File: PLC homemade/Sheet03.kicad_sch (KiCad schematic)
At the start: 54 parts, among them J1 M20-7820646, J16 Conn_01x04, J17 Conn_01x02, U11 GP8403-TC50-EW_C3152007, U12 MAX13487EESAT, U13 SMBJ7.0CA-Q, U14 SMBJ7.0CA-Q, U4 LM324ADT, U5 SN74LVC1G125DRL, U6 SN74LVC1G125DRL

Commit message: :tada: Run Electrical rule checker All errors corrected
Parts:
- C21, C22, C23, C24, C25, C26, C28, C42, C43, C45, C46: footprint (none) -> Capacitor_SMD:C_01005_0402Metric
- C27, C41, C44, C47, C48: footprint (none) -> Capacitor_SMD:C_0201_0603Metric
- J1: footprint (none) -> M20-7820646:HARWIN_M20-7820646
- J16: footprint (none) -> Connector_PinHeader_2.00mm:PinHeader_1x04_P2.00mm_Vertical
- J17: footprint (none) -> Connector_PinHeader_2.00mm:PinHeader_1x02_P2.00mm_Vertical
- L2, L3: footprint (none) -> Inductor_SMD:L_APV_APH1040
- R23, R29, R30, R32, R33, R34, R35, R66: footprint (none) -> Resistor_SMD:R_1206_3216Metric
- R24, R25, R26, R27, R28, R31, R65, R67, R68: footprint (none) -> Resistor_SMD:R_01005_0402Metric
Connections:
- net INPUT_AAA0 is gone; now on net INPUT_AA0: U4.2 (NEG_1)
- net INPUT_AAA1 is gone; now on net INPUT_AA1: U4.6 (NEG_2)
- net INPUT_AAA2 is gone; now on net INPUT_AA2: U4.9 (NEG3)
- net INPUT_AAA3 is gone; now on net INPUT_AA3: U4.13 (NEG_4)
- net AGND: now also U6.3 (GND)
- no-connect marks 0 -> 1
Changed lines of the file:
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@@
 		(color 0 0 0 0)
 	)
+	(no_connect
+		(at 231.14 266.7)
+	)
 	(wire
 		(pts
@@
 	(wire
 		(pts
+			(xy 232.41 213.36) (xy 232.41 215.9)
+		)
+		(stroke
+			(width 0)
+			(type default)
+		)
+	)
+	(wire
+		(pts
 			(xy 114.3 210.82) (xy 114.3 217.17)
 		)
@@
 		)
 	)
-	(label "INPUT_AAA0"
+	(label "INPUT_AA0"
 		(at 81.28 40.64 0)
 		(effects
@@
 		)
 	)
-	(label "INPUT_AAA1"
+	(label "INPUT_AA1"
 		(at 81.28 45.72 0)
 		(effects
@@
 		)
 	)
-	(label "INPUT_AAA2"
+	(label "INPUT_AA2"
 		(at 81.28 50.8 0)
 		(effects
@@
 		)
 	)
-	(label "INPUT_AAA3"
+	(label "INPUT_AA3"
 		(at 81.28 55.88 0)
 		(effects
@@
 		)
 	)
+	(global_label "4G_RX"
+		(shape input)
+		(at 223.52 261.62 180)
+		(fields_autoplaced yes)
+		(effects
+			(font
+				(size 1.27 1.27)
+			)
+			(justify right)
+		)
+		(property "Intersheetrefs" "${INTERSHEET_REFS}"
+			(at 214.6082 261.62 0)
+			(effects
+				(font
+					(size 1.27 1.27)
+				)
+				(justify right)
+				(hide yes)
+			)
+		)
+	)
 	(global_label "INA3"
 		(shape input)
@@
 		)
 	)
-	(hierarchical_label "4G_TX"
+	(global_label "4G_TX"
 		(shape input)
 		(at 223.52 264.16 180)
+		(fields_autoplaced yes)
 		(effects
 			(font
@@
 			(justify right)
 		)
-	)
-	(hierarchical_label "4G_RX"
-		(shape input)
-		(at 223.52 261.62 180)
-		(effects
-			(font
-				(size 1.27 1.27)
+		(property "Intersheetrefs" "${INTERSHEET_REFS}"
+			(at 214.9106 264.16 0)
+			(effects
+				(font
+					(size 1.27 1.27)
+				)
+				(justify right)
+				(hide yes)
 			)
-			(justify right)
 		)
 	)
@@
 			)
 		)
-		(property "Footprint" ""
+		(property "Footprint" "Capacitor_SMD:C_01005_0402Metric"
 			(at 139.3952 153.67 0)
 			(effects
@@
 			)
 		)
-		(property "Footprint" ""
+		(property "Footprint" "Inductor_SMD:L_APV_APH1040"
 			(at 38.1 129.54 0)
 			(effects
@@
 			)
 		)
-		(property "Footprint" ""
+		(property "Footprint" "Capacitor_SMD:C_01005_0402Metric"
 			(at 171.1452 157.48 0)
 			(effects
@@
 			)
 		)
-		(property "Footprint" ""
+		(property "Footprint" "Connector_PinHeader_2.00mm:PinHeader_1x04_P2.00mm_Vertical"
 			(at 177.8 91.44 0)
 			(effects
@@
 			)
 		)
-		(property "Footprint" ""
+		(property "Footprint" "Resistor_SMD:R_01005_0402Metric"
 			(at 188.722 39.37 90)
 			(effects
@@
 			)
 		)
-		(property "Footprint" ""
+		(property "Footprint" "Capacitor_SMD:C_01005_0402Metric"
 			(at 72.0852 140.97 0)
 			(effects
@@
 			)
 		)
-		(property "Footprint" ""
+		(property "Footprint" "Capacitor_SMD:C_01005_0402Metric"
 			(at 228.2952 41.91 0)
 			(effects
@@
 			)
 		)
-		(property "Footprint" ""
+		(property "Footprint" "Capacitor_SMD:C_0201_0603Metric"
 			(at 134.9248 121.92 0)
 			(effects
@@
 			)
 		)
-		(property "Footprint" ""
+		(property "Footprint" "Resistor_SMD:R_1206_3216Metric"
 			(at 176.022 72.39 90)
 			(effects
@@
 			)
 		)
-		(property "Footprint" ""
+		(property "Footprint" "Resistor_SMD:R_01005_0402Metric"
 			(at 31.75 217.678 90)
 			(effects
@@
 			)
 		)
-		(property "Footprint" ""
+		(property "Footprint" "Resistor_SMD:R_1206_3216Metric"
 			(at 173.99 33.528 90)
 			(effects
@@
 			)
 		)
-		(property "Footprint" ""
+		(property "Footprint" "Connector_PinHeader_2.00mm:PinHeader_1x02_P2.00mm_Vertical"
 			(at 69.85 162.56 0)
 			(effects
@@
 			)
 		)
-		(property "Footprint" ""
+		(property "Footprint" "Resistor_SMD:R_1206_3216Metric"
 			(at 106.68 212.598 90)
 			(effects
@@
 			)
 		)
-		(property "Footprint" ""
+		(property "Footprint" "Capacitor_SMD:C_0201_0603Metric"
 			(at 49.2252 43.18 0)
 			(effects
@@
 			)
 		)
-		(property "Footprint" ""
+		(property "Footprint" "Resistor_SMD:R_1206_3216Metric"
 			(at 226.06 249.428 90)
 			(effects
@@
 			)
 		)
-		(property "Footprint" ""
+		(property "Footprint" "M20-7820646:HARWIN_M20-7820646"
 			(at 236.22 264.16 0)
 			(effects
@@
 			)
 		)
-		(property "Footprint" ""
+		(property "Footprint" "Resistor_SMD:R_1206_3216Metric"
 			(at 227.33 234.188 90)
 			(effects
@@
 			)
 		)
-		(property "Footprint" ""
+		(property "Footprint" "Capacitor_SMD:C_01005_0402Metric"
 			(at 199.0852 77.47 0)
 			(effects
@@
 			)
 		)
-		(property "Footprint" ""
+		(property "Footprint" "Capacitor_SMD:C_01005_0402Metric"
 			(at 243.5352 76.2 0)
 			(effects
@@
 			)
 		)
-		(property "Footprint" ""
+		(property "Footprint" "Capacitor_SMD:C_0201_0603Metric"
 			(at 47.9552 262.89 0)
 			(effects
@@
 			)
 		)
-		(property "Footprint" ""
+		(property "Footprint" "Resistor_SMD:R_01005_0402Metric"
 			(at 93.98 226.568 90)
 			(effects
@@
 			)
 		)
-		(property "Footprint" ""
+		(property "Footprint" "Resistor_SMD:R_1206_3216Metric"
 			(at 224.282 71.12 90)
 			(effects
@@
 			)
 		)
-		(property "Footprint" ""
+		(property "Footprint" "Resistor_SMD:R_01005_0402Metric"
 			(at 185.42 67.818 90)
 			(effects
@@
 			)
 		)
-		(property "Footprint" ""
+		(property "Footprint" "Capacitor_SMD:C_0201_0603Metric"
 			(at 58.1152 139.7 0)
 			(effects
@@
 			)
 		)
-		(property "Footprint" ""
+		(property "Footprint" "Capacitor_SMD:C_01005_0402Metric"
 			(at 181.3052 41.91 0)
 			(effects
@@
 			)
 		)
-		(property "Footprint" ""
+		(property "Footprint" "Resistor_SMD:R_1206_3216Metric"
 			(at 242.57 230.378 90)
 			(effects
@@
 			)
 		)
-		(property "Footprint" ""
+		(property "Footprint" "Capacitor_SMD:C_01005_0402Metric"
 			(at 31.4452 262.89 0)
 			(effects
@@
 			)
 		)
-		(property "Footprint" ""
+		(property "Footprint" "Resistor_SMD:R_01005_0402Metric"
 			(at 106.68 260.858 90)
 			(effects
@@
 			)
 		)
-		(property "Footprint" ""
+		(property "Footprint" "Capacitor_SMD:C_0201_0603Metric"
 			(at 63.1952 44.45 0)
 			(effects
@@
 			)
 		)
-		(property "Footprint" ""
+		(property "Footprint" "Resistor_SMD:R_01005_0402Metric"
 			(at 235.712 39.37 90)
 			(effects
@@
 			)
 		)
-		(property "Footprint" ""
+		(property "Footprint" "Capacitor_SMD:C_01005_0402Metric"
 			(at 129.54 241.6048 0)
 			(effects
@@
 			)
 		)
-		(property "Footprint" ""
+		(property "Footprint" "Resistor_SMD:R_1206_3216Metric"
 			(at 241.3 245.618 90)
 			(effects
@@
 			)
 		)
-		(property "Footprint" ""
+		(property "Footprint" "Capacitor_SMD:C_01005_0402Metric"
 			(at 100.0252 156.21 0)
 			(effects
@@
 			)
 		)
-		(property "Footprint" ""
+		(property "Footprint" "Capacitor_SMD:C_01005_0402Metric"
 			(at 223.52 185.7248 0)
 			(effects
@@
 			)
 		)
-		(property "Footprint" ""
+		(property "Footprint" "Resistor_SMD:R_01005_0402Metric"
 			(at 233.68 66.548 90)
 			(effects
@@
 			)
 		)
-		(property "Footprint" ""
+		(property "Footprint" "Inductor_SMD:L_APV_APH1040"
 			(at 29.21 33.02 0)
 			(effects
@@
 			)
 		)
-		(property "Footprint" ""
+		(property "Footprint" "Resistor_SMD:R_01005_0402Metric"
 			(at 220.98 33.528 90)
 			(effects
@@
 			)
 		)
-		(property "Footprint" ""
+		(property "Footprint" "Resistor_SMD:R_01005_0402Metric"
 			(at 93.98 204.978 90)
 			(effects

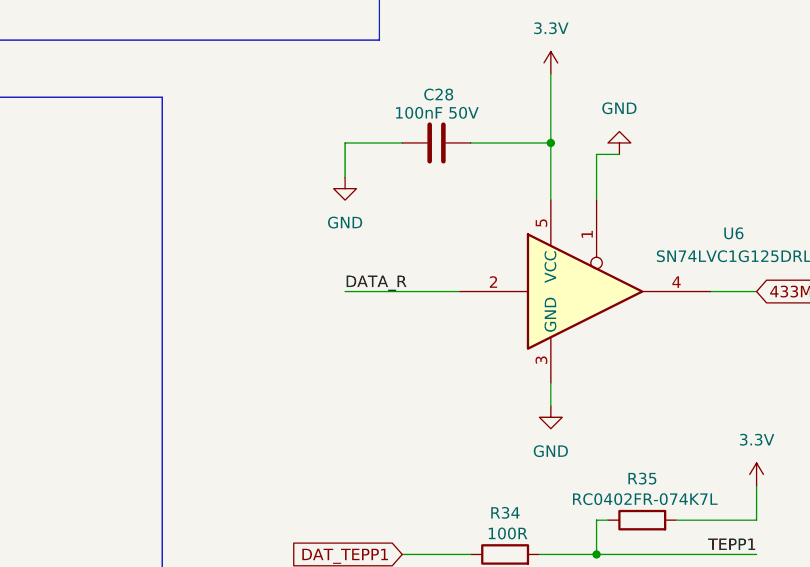
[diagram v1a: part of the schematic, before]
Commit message: :memo: Started On editor , Ethernet and Power Sector
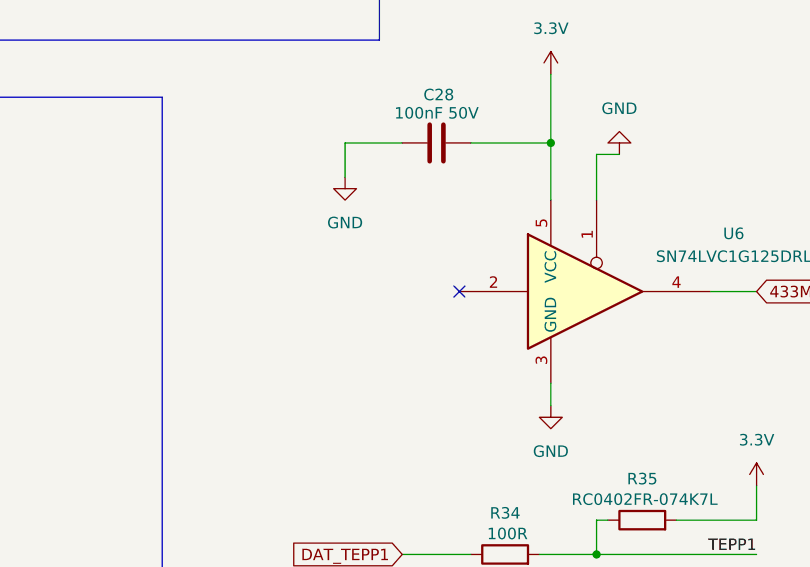
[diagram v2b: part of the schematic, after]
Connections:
- net DATA_R: no longer names the net of U6.2
- no-connect marks 1 -> 2
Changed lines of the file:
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@@
+	)
+	(no_connect
+		(at 222.25 203.2)
 	)
 	(no_connect
@@
 		(pts
 			(xy 226.06 64.77) (xy 226.06 67.31)
-		)
-		(stroke
-			(width 0)
-			(type default)
-		)
-	)
-	(wire
-		(pts
-			(xy 209.55 203.2) (xy 222.25 203.2)
 		)
 		(stroke
@@
 		)
 	)
-	(label "DATA_R"
-		(at 209.55 203.2 0)
-		(effects
-			(font
-				(size 1.27 1.27)
-			)
-			(justify left bottom)
-		)
-	)

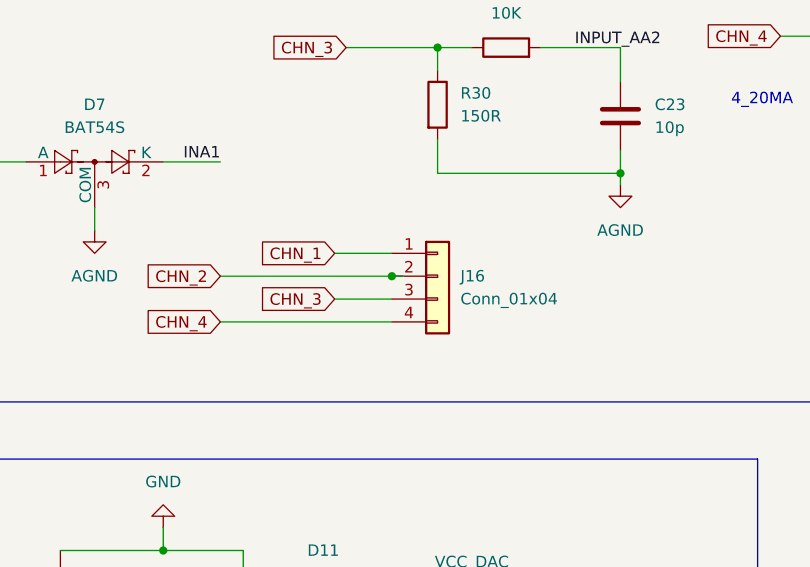
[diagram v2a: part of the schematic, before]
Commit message: :ambulance:2output and usbc
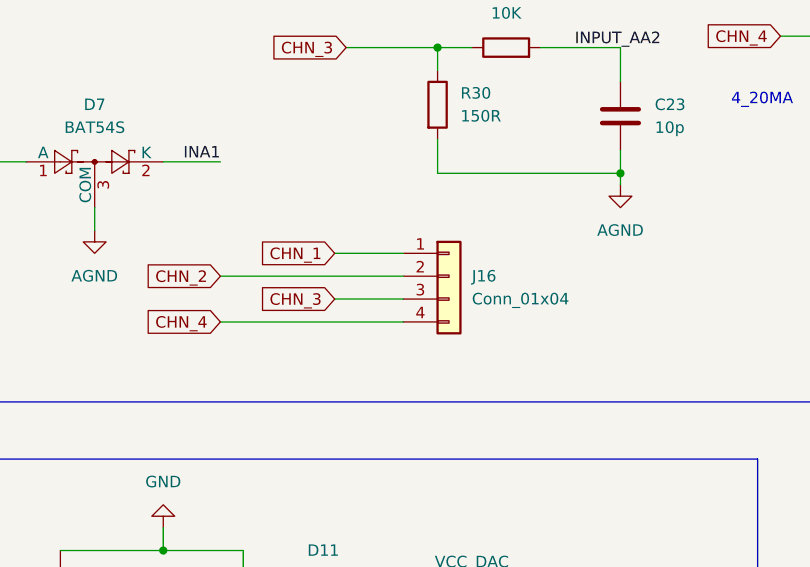
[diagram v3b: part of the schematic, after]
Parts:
- R25: footprint Resistor_SMD:R_01005_0402Metric -> Resistor_SMD:R_1206_3216Metric
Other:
- moved on the sheet: J16
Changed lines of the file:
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@@
 	)
 	(junction
-		(at 172.72 91.44)
-		(diameter 0)
-		(color 0 0 0 0)
-	)
-	(junction
 		(at 232.41 46.99)
 		(diameter 0)
@@
 	(wire
 		(pts
-			(xy 166.37 93.98) (xy 172.72 93.98)
+			(xy 166.37 93.98) (xy 173.99 93.98)
 		)
 		(stroke
@@
 	(wire
 		(pts
-			(xy 153.67 91.44) (xy 172.72 91.44)
+			(xy 153.67 91.44) (xy 173.99 91.44)
 		)
 		(stroke
@@
 	(wire
 		(pts
-			(xy 166.37 88.9) (xy 172.72 88.9)
+			(xy 166.37 88.9) (xy 173.99 88.9)
 		)
 		(stroke
@@
 	(wire
 		(pts
-			(xy 153.67 96.52) (xy 172.72 96.52)
+			(xy 153.67 96.52) (xy 173.99 96.52)
 		)
 		(stroke
@@
 	(wire
 		(pts
-			(xy 172.72 91.44) (xy 173.99 91.44)
-		)
-		(stroke
-			(width 0)
-			(type default)
-		)
-	)
-	(wire
-		(pts
 			(xy 130.81 142.24) (xy 133.35 142.24)
 		)
@@
 	(symbol
 		(lib_id "Connector_Generic:Conn_01x04")
-		(at 177.8 91.44 0)
+		(at 179.07 91.44 0)
 		(unit 1)
 		(exclude_from_sim no)
@@
 		(fields_autoplaced yes)
 		(property "Reference" "J16"
-			(at 180.34 91.4399 0)
+			(at 181.61 91.4399 0)
 			(effects
 				(font
@@
 		)
 		(property "Value" "Conn_01x04"
-			(at 180.34 93.9799 0)
+			(at 181.61 93.9799 0)
 			(effects
 				(font
@@
 		)
 		(property "Footprint" "Connector_PinHeader_2.00mm:PinHeader_1x04_P2.00mm_Vertical"
-			(at 177.8 91.44 0)
+			(at 179.07 91.44 0)
 			(effects
 				(font
@@
 		)
 		(property "Datasheet" "~"
-			(at 177.8 91.44 0)
+			(at 179.07 91.44 0)
 			(effects
 				(font
@@
 		)
 		(property "Description" "Generic connector, single row, 01x04, script generated (kicad-library-utils/schlib/autogen/connector/)"
-			(at 177.8 91.44 0)
+			(at 179.07 91.44 0)
 			(effects
 				(font
@@
 			)
 		)
-		(property "Footprint" "Resistor_SMD:R_01005_0402Metric"
+		(property "Footprint" "Resistor_SMD:R_1206_3216Metric"
 			(at 220.98 33.528 90)
 			(effects

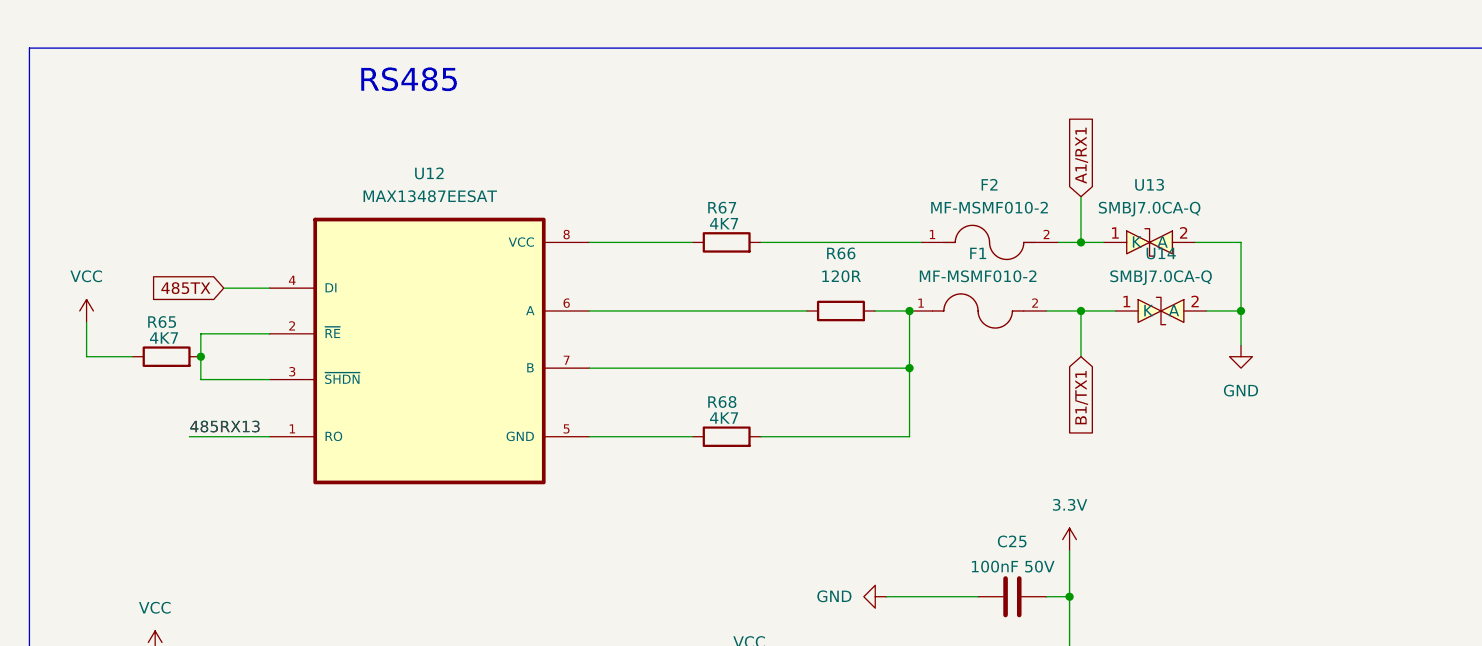
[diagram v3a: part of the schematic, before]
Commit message: :ambulance: Changed the 5 footprint error
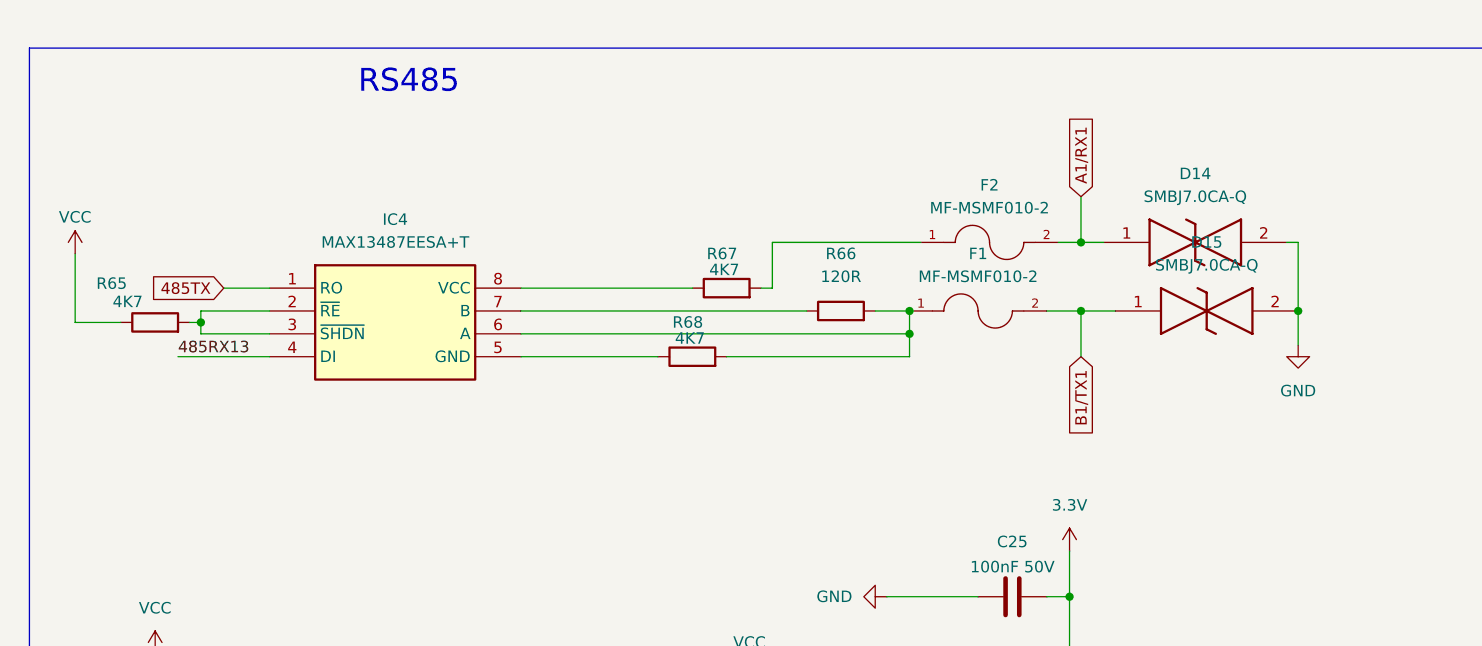
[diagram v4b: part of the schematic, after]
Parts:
- removed U12: MAX13487EESAT, MAX13487EESAT:SOIC127P600X175-8N, symbol MAX13487EESAT:MAX13487EESAT
- removed U13, U14: SMBJ7.0CA-Q, SMBJ7:SMB_L4.3-W3.6-LS5.4-BI, symbol SMBJ7.0CA-Q:SMBJ7.0CA-Q
- added D14, D15: SMBJ7.0CA-Q, DIONM5436X244N, symbol SMBJ7_0CA-Q:SMBJ7.0CA-Q
- added IC4: MAX13487EESA+T, SOIC127P600X175-8N, symbol MAX13487EESA+T:MAX13487EESA+T
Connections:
- net 485RX13: now also IC4.4 (DI)
- net 485TX: now also IC4.1 (RO)
- net A1/RX1: now also D14.1
- net AGND: now also D14.2, D15.2
- net B1/TX1: now also D15.1
- net at F1.1, R66.2, R68.2: now also IC4.6 (A)
- net at R65.2: now also IC4.2 (~{RE}), IC4.3 (~{SHDN})
- net at R68.1: now also IC4.5 (GND)
- net at R66.1: now also IC4.7 (B)
- net at R67.1: now also IC4.8 (VCC)
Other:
- moved on the sheet: R65, R67, R68

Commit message: :art: wiring componets done
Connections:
- net II_SDA renamed IIC_SDA
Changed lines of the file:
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@@
-		)
-	)
-	(global_label "II_SDA"
-		(shape input)
-		(at 102.87 134.62 180)
-		(fields_autoplaced yes)
-		(effects
-			(font
-				(size 1.27 1.27)
-			)
-			(justify right)
-		)
-		(property "Intersheetrefs" "${INTERSHEET_REFS}"
-			(at 94.1395 134.62 0)
-			(effects
-				(font
-					(size 1.27 1.27)
-				)
-				(justify right)
-				(hide yes)
-			)
 		)
 	)
@@
 			(effects
 				(font
+					(size 1.27 1.27)
+				)
+				(justify right)
+				(hide yes)
+			)
+		)
+	)
+	(global_label "IIC_SDA"
+		(shape input)
+		(at 102.87 134.62 180)
+		(fields_autoplaced yes)
+		(effects
+			(font
+				(size 1.27 1.27)
+			)
+			(justify right)
+		)
+		(property "Intersheetrefs" "${INTERSHEET_REFS}"
+			(at 92.8695 134.62 0)
+			(effects
+				(font
